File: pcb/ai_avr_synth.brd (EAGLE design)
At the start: 99.1 x 69.8 mm, 45 parts, among them IC1 ATMEGA328P-PDIP, J1 1X02ST, J2 1X06, J3 1X08, J4 1X08, J5 MIDIJACK, J6 STEREOJACKSJ1-3555NG, U1 MC7805, U2 TLC2262, U3 6N138

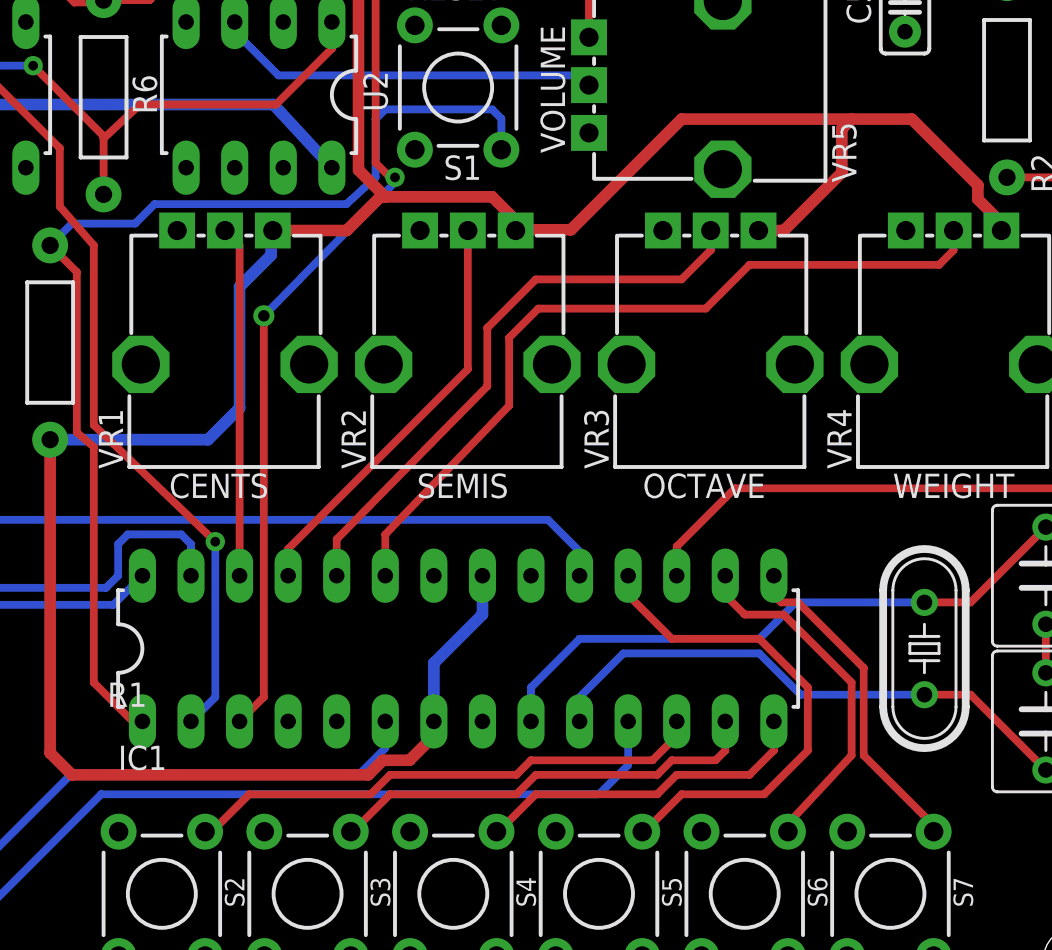
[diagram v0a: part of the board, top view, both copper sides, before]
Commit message: Updated components to use the latest libraries.  Had to redo a few traces (nothing major)
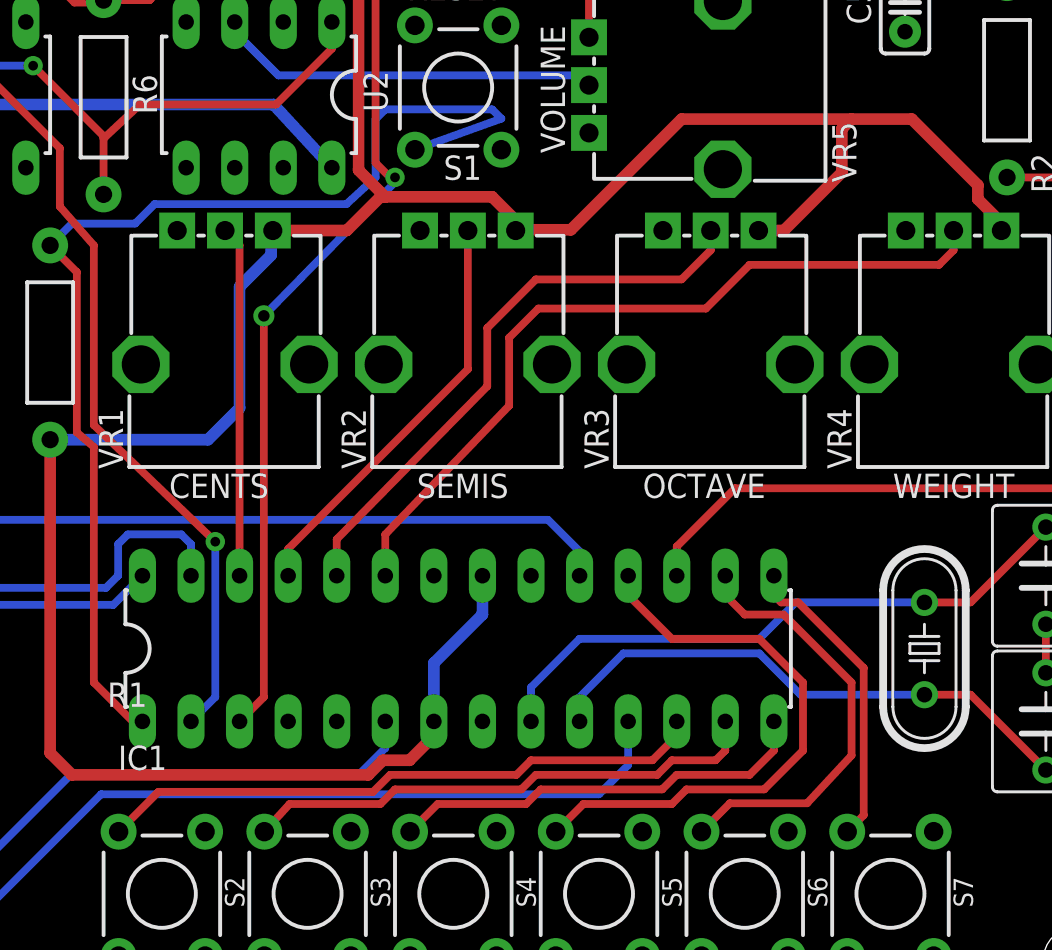
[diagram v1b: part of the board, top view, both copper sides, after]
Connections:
- net BTN_BANK: now also S5.A@1; no longer S5.B@1
- net BTN_EXTRA: now also S7.A@1; no longer S7.B@1
- net BTN_LOCK: now also S6.A@1; no longer S6.B@1
- net BTN_OSC1: now also S2.A@1; no longer S2.B@1
- net BTN_OSC2: now also S3.A@1; no longer S3.B@1
- net BTN_SAVE: now also S4.A@1; no longer S4.B@1
- net GND: now also S1.A@1, S2.B@1, S3.B@1, S4.B@1, S5.B@1, S6.B@1, S7.B@1; no longer S1.B@1, S2.A@1, S3.A@1, S4.A@1, S5.A@1, S6.A@1, S7.A@1
- net RESET: now also S1.B@1; no longer S1.A@1
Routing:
- net BTN_OSC2: track 22.9 -> 27.4 mm
- net BTN_SAVE: track 17.8 -> 22.3 mm
- net BTN_OSC1: track 27.5 -> 32.0 mm
- net BTN_LOCK: track 18.6 -> 22.9 mm
- net BTN_BANK: track 26.1 -> 30.3 mm
- net RESET: track 57.3 -> 60.5 mm
- net BTN_EXTRA: track 17.4 -> 16.2 mm
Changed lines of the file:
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@@
 <contactref element="C1" pad="C"/>
 <contactref element="C2" pad="C"/>
-<contactref element="S1" pad="B@1"/>
+<contactref element="S1" pad="A@1"/>
 <contactref element="IC1" pad="22"/>
 <contactref element="IC1" pad="8"/>
@@
 <contactref element="U2" pad="4"/>
 <contactref element="J6" pad="GND"/>
-<contactref element="S7" pad="A@1"/>
-<contactref element="S6" pad="A@1"/>
-<contactref element="S5" pad="A@1"/>
-<contactref element="S4" pad="A@1"/>
-<contactref element="S3" pad="A@1"/>
-<contactref element="S2" pad="A@1"/>
+<contactref element="S7" pad="B@1"/>
+<contactref element="S6" pad="B@1"/>
+<contactref element="S5" pad="B@1"/>
+<contactref element="S4" pad="B@1"/>
+<contactref element="S3" pad="B@1"/>
+<contactref element="S2" pad="B@1"/>
 <contactref element="J1" pad="2"/>
 <contactref element="C3" pad="2"/>
@@
 <signal name="RESET">
 <contactref element="IC1" pad="1"/>
-<contactref element="S1" pad="A@1"/>
+<contactref element="S1" pad="B@1"/>
 <contactref element="R1" pad="P$1"/>
 <wire x1="42.926" y1="39.878" x2="44.069" y2="41.021" width="0.4064" layer="16"/>
@@
 <wire x1="60.452" y1="46.99" x2="66.04" y2="46.99" width="0.4064" layer="16"/>
 <wire x1="66.04" y1="46.99" x2="66.5226" y2="46.5074" width="0.4064" layer="16"/>
-<wire x1="66.5226" y1="46.5074" x2="66.5226" y2="44.8818" width="0.4064" layer="16"/>
+<wire x1="66.5226" y1="46.5074" x2="62.0014" y2="44.8818" width="0.4064" layer="16"/>
 <wire x1="45.212" y1="29.337" x2="45.212" y2="17.018" width="0.4064" layer="1"/>
 <wire x1="45.212" y1="17.018" x2="47.244" y2="14.986" width="0.4064" layer="1"/>
@@
 <signal name="BTN_SAVE">
 <contactref element="IC1" pad="14"/>
-<contactref element="S4" pad="B@1"/>
-<wire x1="66.2686" y1="9.2202" x2="66.3702" y2="9.2202" width="0.4064" layer="1"/>
-<wire x1="66.3702" y1="9.2202" x2="68.326" y2="11.176" width="0.4064" layer="1"/>
-<wire x1="68.326" y1="11.176" x2="74.676" y2="11.176" width="0.4064" layer="1"/>
-<wire x1="74.676" y1="11.176" x2="75.692" y2="12.192" width="0.4064" layer="1"/>
+<contactref element="S4" pad="A@1"/>
+<wire x1="68.58" y1="11.43" x2="74.93" y2="11.43" width="0.4064" layer="1"/>
+<wire x1="74.93" y1="11.43" x2="75.692" y2="12.192" width="0.4064" layer="1"/>
 <wire x1="75.692" y1="12.192" x2="79.502" y2="12.192" width="0.4064" layer="1"/>
 <wire x1="79.502" y1="12.192" x2="80.772" y2="13.462" width="0.4064" layer="1"/>
 <wire x1="80.772" y1="13.462" x2="80.772" y2="14.986" width="0.4064" layer="1"/>
+<wire x1="61.7474" y1="9.2202" x2="63.1952" y2="10.668" width="0.4064" layer="1"/>
+<wire x1="63.1952" y1="10.668" x2="67.818" y2="10.668" width="0.4064" layer="1"/>
+<wire x1="67.818" y1="10.668" x2="68.58" y2="11.43" width="0.4064" layer="1"/>
 </signal>
 <signal name="CENTS">
@@
 <signal name="BTN_OSC1">
 <contactref element="IC1" pad="12"/>
-<contactref element="S2" pad="B@1"/>
-<wire x1="51.0286" y1="9.2202" x2="51.3842" y2="9.2202" width="0.4064" layer="1"/>
-<wire x1="51.3842" y1="9.2202" x2="53.34" y2="11.176" width="0.4064" layer="1"/>
-<wire x1="53.34" y1="11.176" x2="59.69" y2="11.176" width="0.4064" layer="1"/>
-<wire x1="59.69" y1="11.176" x2="60.706" y2="12.192" width="0.4064" layer="1"/>
+<contactref element="S2" pad="A@1"/>
+<wire x1="48.5902" y1="11.303" x2="59.817" y2="11.303" width="0.4064" layer="1"/>
+<wire x1="59.817" y1="11.303" x2="60.706" y2="12.192" width="0.4064" layer="1"/>
 <wire x1="60.706" y1="12.192" x2="67.31" y2="12.192" width="0.4064" layer="1"/>
 <wire x1="67.31" y1="12.192" x2="68.072" y2="12.954" width="0.4064" layer="1"/>
@@
 <wire x1="74.422" y1="12.954" x2="75.692" y2="14.224" width="0.4064" layer="1"/>
 <wire x1="75.692" y1="14.224" x2="75.692" y2="14.986" width="0.4064" layer="1"/>
+<wire x1="46.5074" y1="9.2202" x2="48.5902" y2="11.303" width="0.4064" layer="1"/>
 </signal>
 <signal name="BTN_OSC2">
 <contactref element="IC1" pad="13"/>
-<contactref element="S3" pad="B@1"/>
-<wire x1="58.6486" y1="9.2202" x2="58.7502" y2="9.2202" width="0.4064" layer="1"/>
-<wire x1="58.7502" y1="9.2202" x2="60.706" y2="11.176" width="0.4064" layer="1"/>
-<wire x1="60.706" y1="11.176" x2="67.31" y2="11.176" width="0.4064" layer="1"/>
-<wire x1="67.31" y1="11.176" x2="68.326" y2="12.192" width="0.4064" layer="1"/>
+<contactref element="S3" pad="A@1"/>
+<wire x1="60.96" y1="11.43" x2="67.564" y2="11.43" width="0.4064" layer="1"/>
+<wire x1="67.564" y1="11.43" x2="68.326" y2="12.192" width="0.4064" layer="1"/>
 <wire x1="68.326" y1="12.192" x2="74.676" y2="12.192" width="0.4064" layer="1"/>
 <wire x1="74.676" y1="12.192" x2="75.438" y2="12.954" width="0.4064" layer="1"/>
@@
 <wire x1="77.724" y1="12.954" x2="78.232" y2="13.462" width="0.4064" layer="1"/>
 <wire x1="78.232" y1="13.462" x2="78.232" y2="14.986" width="0.4064" layer="1"/>
+<wire x1="54.1274" y1="9.2202" x2="55.4482" y2="10.668" width="0.4064" layer="1"/>
+<wire x1="55.4482" y1="10.668" x2="60.198" y2="10.668" width="0.4064" layer="1"/>
+<wire x1="60.198" y1="10.668" x2="60.96" y2="11.43" width="0.4064" layer="1"/>
 </signal>
 <signal name="BTN_BANK">
-<contactref element="S5" pad="B@1"/>
+<contactref element="S5" pad="A@1"/>
 <contactref element="IC1" pad="18"/>
 <wire x1="73.152" y1="22.606" x2="73.152" y2="21.59" width="0.4064" layer="1"/>
 <wire x1="73.152" y1="21.59" x2="75.438" y2="19.304" width="0.4064" layer="1"/>
 <wire x1="75.438" y1="19.304" x2="80.01" y2="19.304" width="0.4064" layer="1"/>
-<wire x1="80.01" y1="19.304" x2="82.55" y2="16.764" width="0.4064" layer="1"/>
-<wire x1="82.55" y1="16.764" x2="82.55" y2="13.462" width="0.4064" layer="1"/>
-<wire x1="82.55" y1="13.462" x2="80.264" y2="11.176" width="0.4064" layer="1"/>
-<wire x1="80.264" y1="11.176" x2="75.946" y2="11.176" width="0.4064" layer="1"/>
-<wire x1="75.946" y1="11.176" x2="73.9902" y2="9.2202" width="0.4064" layer="1"/>
-<wire x1="73.9902" y1="9.2202" x2="73.8886" y2="9.2202" width="0.4064" layer="1"/>
+<wire x1="80.01" y1="19.304" x2="82.296" y2="17.018" width="0.4064" layer="1"/>
+<wire x1="82.296" y1="17.018" x2="82.296" y2="13.462" width="0.4064" layer="1"/>
+<wire x1="82.296" y1="13.462" x2="80.264" y2="11.43" width="0.4064" layer="1"/>
+<wire x1="80.264" y1="11.43" x2="76.2" y2="11.43" width="0.4064" layer="1"/>
+<wire x1="69.3674" y1="9.2202" x2="70.8152" y2="10.668" width="0.4064" layer="1"/>
+<wire x1="70.8152" y1="10.668" x2="75.438" y2="10.668" width="0.4064" layer="1"/>
+<wire x1="75.438" y1="10.668" x2="76.2" y2="11.43" width="0.4064" layer="1"/>
 </signal>
 <signal name="BTN_LOCK">
 <contactref element="IC1" pad="16"/>
-<contactref element="S6" pad="B@1"/>
-<wire x1="81.5086" y1="9.2202" x2="81.5086" y2="9.6266" width="0.4064" layer="1"/>
-<wire x1="81.5086" y1="9.6266" x2="84.836" y2="13.208" width="0.4064" layer="1"/>
+<contactref element="S6" pad="A@1"/>
+<wire x1="82.510359375" y1="10.704828125" x2="84.836" y2="13.208" width="0.4064" layer="1"/>
 <wire x1="84.836" y1="13.208" x2="84.836" y2="17.018" width="0.4064" layer="1"/>
 <wire x1="84.836" y1="17.018" x2="81.28" y2="20.574" width="0.4064" layer="1"/>
@@
 <wire x1="79.248" y1="20.574" x2="78.232" y2="21.59" width="0.4064" layer="1"/>
 <wire x1="78.232" y1="21.59" x2="78.232" y2="22.606" width="0.4064" layer="1"/>
+<wire x1="76.9874" y1="9.2202" x2="78.472028125" y2="10.704828125" width="0.4064" layer="1"/>
+<wire x1="78.472028125" y1="10.704828125" x2="82.510359375" y2="10.704828125" width="0.4064" layer="1"/>
 </signal>
 <signal name="SND_DRT">
@@
 </signal>
 <signal name="BTN_EXTRA">
-<contactref element="S7" pad="B@1"/>
+<contactref element="S7" pad="A@1"/>
 <contactref element="IC1" pad="15"/>
 <wire x1="80.772" y1="22.606" x2="80.772" y2="21.59" width="0.4064" layer="1"/>
@@
 <wire x1="81.153" y1="21.209" x2="82.042" y2="21.209" width="0.4064" layer="1"/>
 <wire x1="82.042" y1="21.209" x2="85.471" y2="17.78" width="0.4064" layer="1"/>
-<wire x1="85.471" y1="17.78" x2="85.471" y2="13.208" width="0.4064" layer="1"/>
-<wire x1="85.471" y1="13.208" x2="89.1286" y2="9.5504" width="0.4064" layer="1"/>
-<wire x1="89.1286" y1="9.5504" x2="89.1286" y2="9.2202" width="0.4064" layer="1"/>
+<wire x1="85.471" y1="17.78" x2="85.471" y2="10.0838" width="0.4064" layer="1"/>
+<wire x1="84.6074" y1="9.2202" x2="85.471" y2="10.0838" width="0.4064" layer="1"/>
 </signal>
 <signal name="LCD_DC">

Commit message: New version with modifications discussed with @humanHardDrive
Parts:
- removed J6: STEREOJACKSJ1-3555NG, Ai_Connectors:SJ1-3555NG
- added 3.5MM: STEREOJACKSJ1-351XNG, Ai_Connectors:SJ1-351XNG
- added C8: 0.1uF, Ai_Passives:CAP-025X050
- added D2: (no value), Ai_DiscreteSemis:TH-1N914
- added ISP: 2X03, Ai_Connectors:2X03
- added S8: SW-SPDTTH, Ai_Electromechanical:SW-SPDT-TH
- added VR6: 10K, Ai_Passives:POT-05X05
- C3, C4: device Ai_Passives:CAP-055X070 -> Ai_Passives:CAP-025X050
- C7: value .1uF -> 0.1uF
- D1: value DIODE1N914 -> (none); device Ai_DiscreteSemis:DIODE-1N914 -> Ai_DiscreteSemis:TH-1N914
- S1, S2, S3, S4, S5, S6, S7: device Ai_Electromechanical:SPST-TH06X06 -> Ai_Electromechanical:SW-SPST-TH06X06
- moved R7 14.7 mm to (52.1, 60.5)
- moved U1 8.39 mm to (7.37, 26.5)
- moved C2 7.06 mm to (9.40, 45.2)
- moved VR4 2.57 mm to (92.7, 33.9)
- moved C5 1.78 mm to (89.4, 52.3)
- moved S4 1.78 mm to (65.8, 5.97)
- moved S5 1.78 mm to (73.4, 5.97)
- moved S7 1.78 mm to (88.6, 5.97)
- moved S2 1.78 mm to (50.5, 5.97)
- moved S3 1.78 mm to (58.2, 5.97)
- moved S6 1.78 mm to (81.0, 5.97)
- moved R4 1.52 mm to (18.7, 45.3)
- moved C1 1.44 mm to (9.40, 50.5)
- moved C3 1.40 mm to (95.0, 21.2), turned to 0 degrees
- moved C4 1.40 mm to (95.0, 16.4), turned to 0 degrees
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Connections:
- new net N$2: C8.1, S2.B@1, S3.B@1, S4.B@1, S5.B@1, S6.B@1, S7.B@1
- new net N$5: J1.1, S8.2
- new net N$7: D2.C, U1.IN
- net 5V: now also ISP.2, VR6.1
- net 9V: now also D2.A, S8.3; no longer J1.1, U1.IN
- net BTN_BANK: now also ISP.1
- net GND: now also 3.5MM.GND, C8.2, ISP.6; no longer J6.GND, S2.B@1, S3.B@1, S4.B@1, S5.B@1, S6.B@1, S7.B@1
- net LCD_DC: now also ISP.3
- net LCD_LED: now also VR6.3
- net N$1: now also J5.5; no longer J5.4
- net N$10: now also J5.4; no longer J5.5
- net RESET: now also ISP.5, J2.6
- net SND_DRT: now also ISP.4
- net SND_OUT: now also 3.5MM.RNG, 3.5MM.TIP; no longer J6.RNG, J6.TIP
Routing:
- net N$2: track 0.00 -> 86.6 mm
- net BTN_BANK: track 30.3 -> 91.8 mm, vias 0 -> 1
- net SND_DRT: track 43.1 -> 86.6 mm
- net RESET: track 60.5 -> 103.0 mm
- net SND_OUT: track 58.6 -> 40.8 mm, vias 2 -> 0
- net N$5: track 0.00 -> 17.4 mm
- net N$15: track 17.0 -> 31.5 mm
- net N$11: track 20.2 -> 33.0 mm
- net LCD_DC: track 104.6 -> 116.5 mm
- net N$1: track 10.2 -> 18.6 mm
- net N$10: track 33.0 -> 25.3 mm
- net 9V: track 71.3 -> 64.6 mm
- net SND_CLN: track 18.5 -> 23.0 mm
- net 5V: track 273.9 -> 269.4 mm
- net N$7: track 0.00 -> 4.06 mm
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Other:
- board text added: "1-VCC"
- board text added: "2-GND"
- board text added: "3-SCE"
- board text added: "3.5mm"
- board text added: "4-RST"
- board text added: "5-D/C"
- board text added: "5V"
- board text added: "6-DN(MOSI)"
- board text added: "7-SCLK"
- board text added: "8-LED"
- board text added: "CTS"
- board text added: "DTR"
- board text added: "GND"
- board text added: "LCD_DC"
- board text added: "LCD_RST"
- board text added: "LCD_SCE"
- board text added: "LCD_SCK"
- board text added: "LCD_SIN"
- board text added: "ON | OFF"
- board text added: "RXD"
- board text added: "TXD"
- board text added: "VCC"
- board text added: "VR6"
- board text added: "v1.1"
- board text removed: "-"
- board text removed: "9V"
- board text removed: "v1.0"

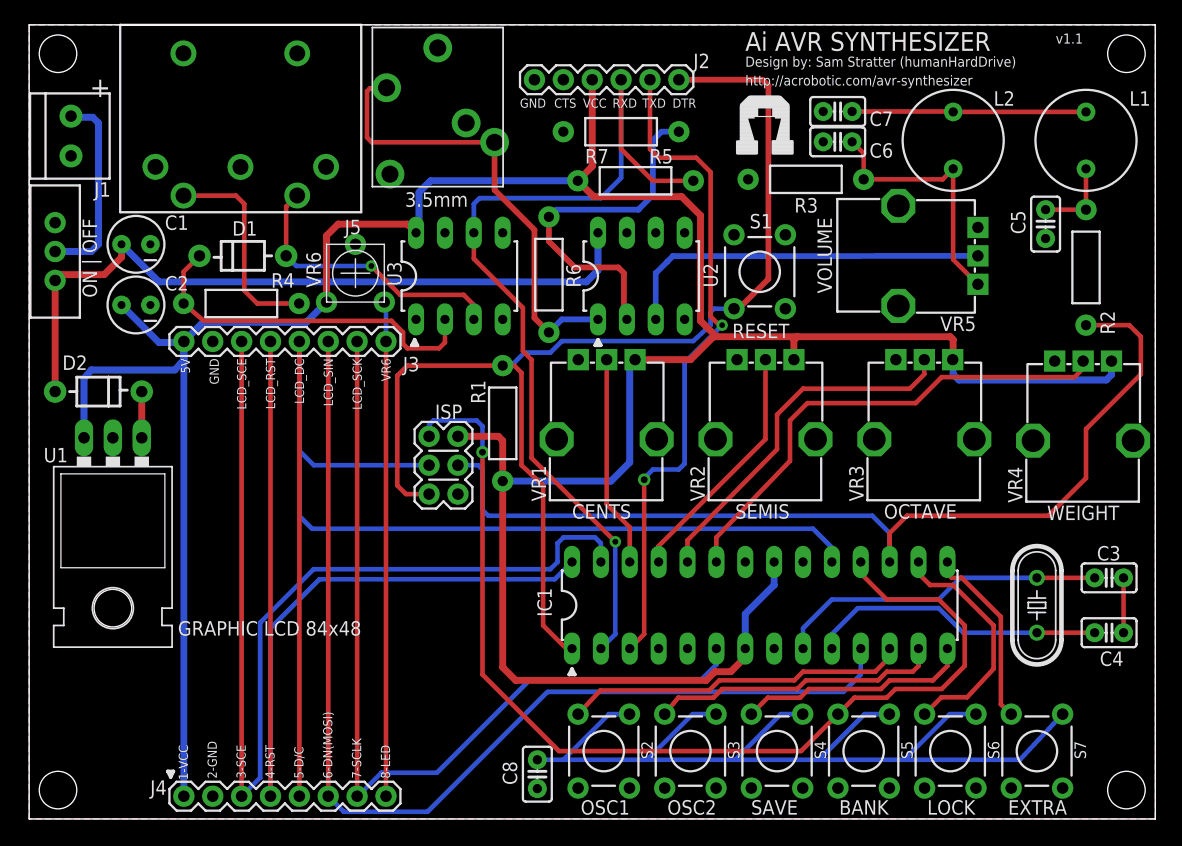
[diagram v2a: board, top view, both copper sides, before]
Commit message: updated a few components
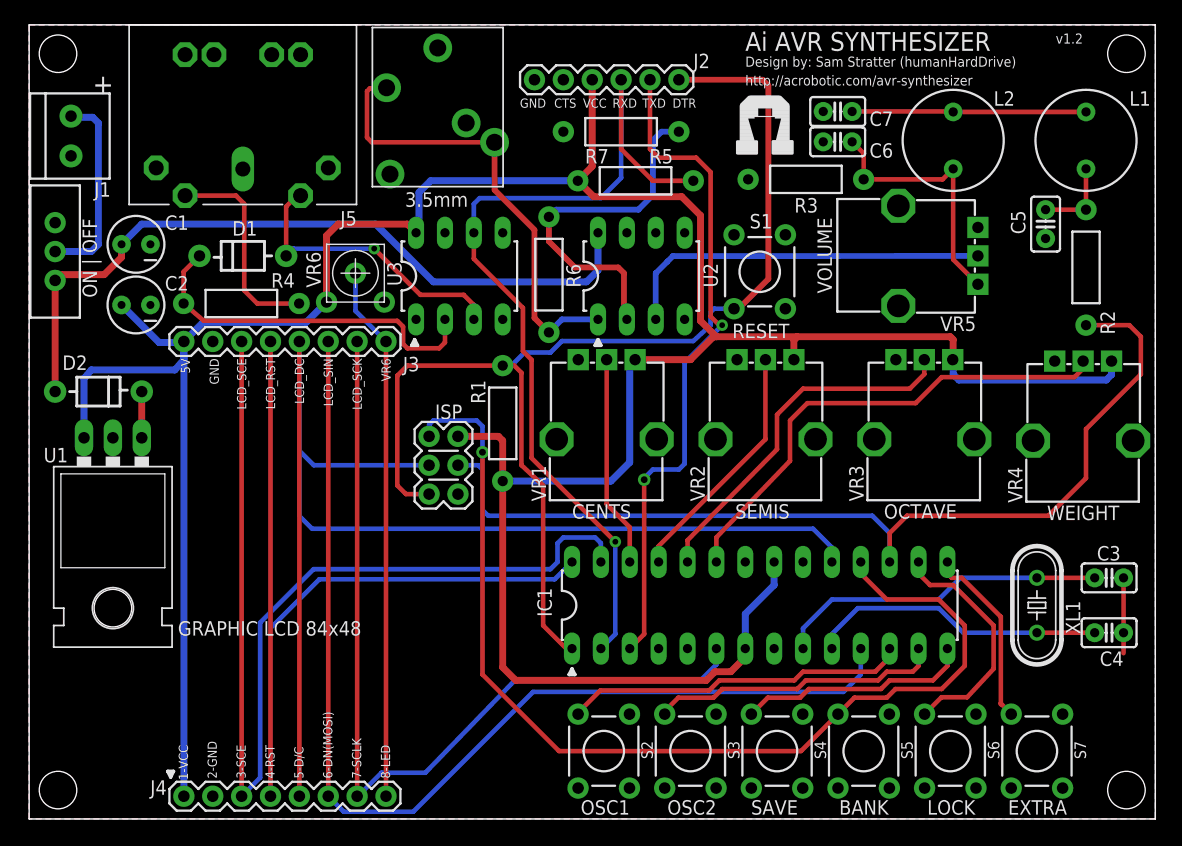
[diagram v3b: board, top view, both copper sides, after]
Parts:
- removed C8: 0.1uF, Ai_Passives:CAP-025X050
- J5: device Ai_Connectors:DIN5 -> Ai_Connectors:CP-2350
- XL1: device Ai_Passives:CRYSTAL-HC49S -> Ai_FrequencyControl:CRYSTAL-HC49S
- moved J5 8.89 mm to (18.8, 69.8)
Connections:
- removed net N$2: C8.1, S2.B@1, S3.B@1, S4.B@1, S5.B@1, S6.B@1, S7.B@1
- net GND: now also S2.B@1, S3.B@1, S4.B@1, S5.B@1, S6.B@1, S7.B@1, VR6.3; no longer C8.2
- net LCD_LED: now also VR6.2; no longer VR6.3
- net N$1: now also J5.4; no longer J5.5
- net N$10: now also J5.5; no longer J5.4
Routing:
- net N$2: track 86.6 -> 0.00 mm
- net LCD_LED: track 43.5 -> 47.1 mm
- net GND: track 4.83 -> 6.63 mm
- net 9V: track 64.6 -> 66.1 mm
- net N$10: track 25.3 -> 26.1 mm
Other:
- board text added: "v1.2"
- board text removed: "v1.1"
